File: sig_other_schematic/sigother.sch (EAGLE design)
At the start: 173 parts, among them IC1 DS3231/SO, IC4 MCP2300X/P, IC5 FT232RLSSOP, K1 TF2-L2-5V, K10 TF2-L2-5V, K11 TF2-L2-5V, K12 TF2-L2-5V, K13 TF2-L2-5V, K14 TF2-L2-5V, K2 TF2-L2-5V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

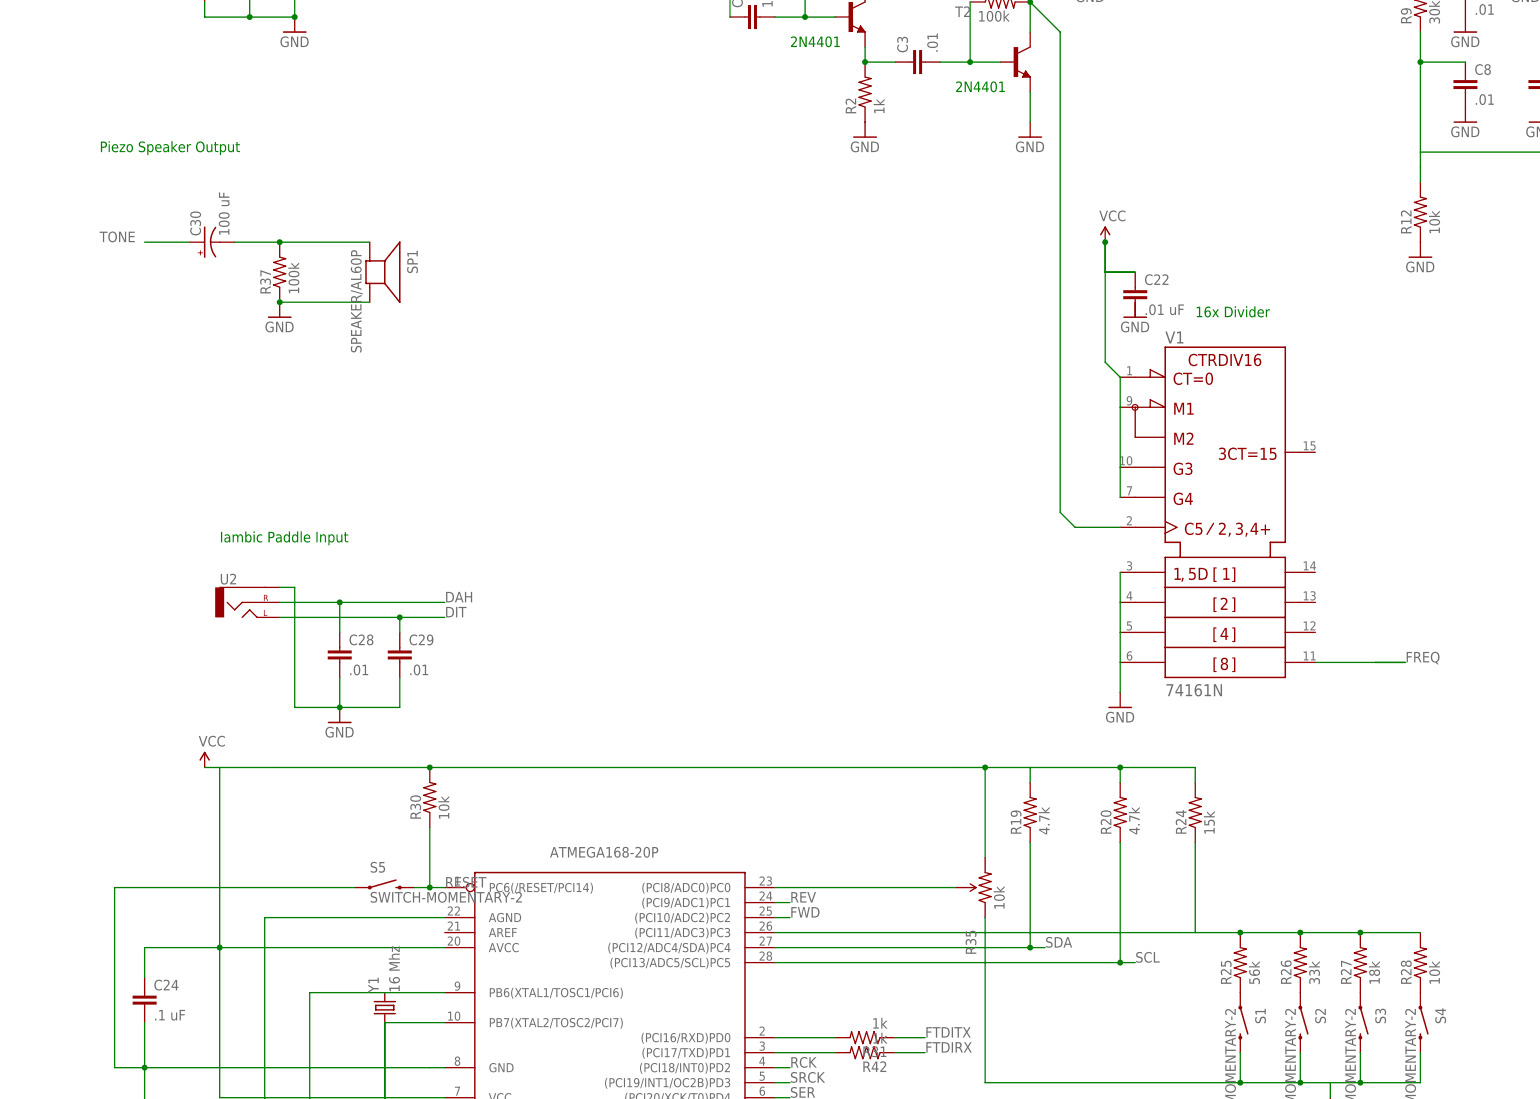
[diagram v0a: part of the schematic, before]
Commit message: updated command button layout (also speaker)
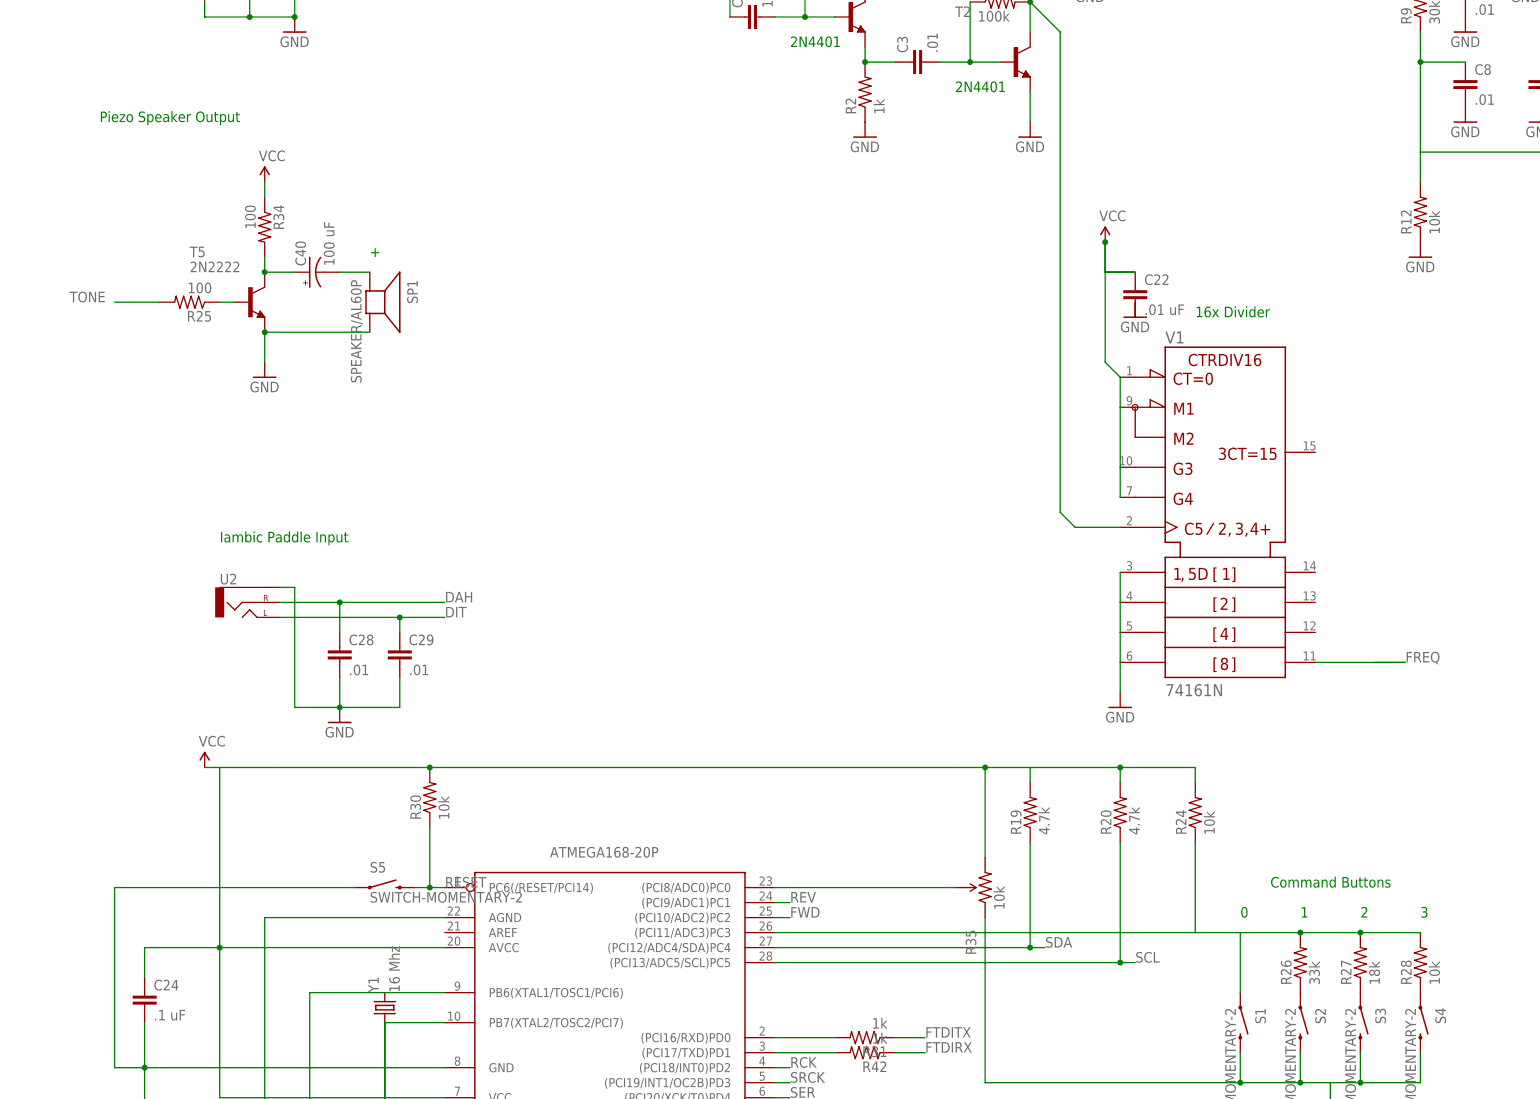
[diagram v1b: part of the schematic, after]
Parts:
- removed C30: 100 uF, SparkFun:CAP_POLPTH1
- removed R37: 100k, SparkFun:RESISTORPTH-1/4W
- added C40: 100 uF, SparkFun:CAP_POLPTH1
- added R34: 100, SparkFun:RESISTORPTH-1/4W
- added T5: 2N2222, adafruit:2N2222
- R24: value 15k -> 10k
- R25: value 56k -> 100
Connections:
- new net N$93: C40.-, SP1.+
- net GND: now also T5.E; no longer R37.1
- net N$104: now also C40.+, R34.2, T5.C; no longer C30.-, R37.2, SP1.+
- net N$12: now also S1.1; no longer R25.2
- net N$65: now also T5.B; no longer S1.1
- net TONE: now also R25.2; no longer C30.+
- net VCC: now also R34.1
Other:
- note added: "+"
- note added: "0"
- note added: "1"
- note added: "2"
- note added: "3"
- note added: "Command Buttons"
- moved on the sheet: R25, SP1
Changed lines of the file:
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@@
 <part name="TPIC6B595" library="ic-package" deviceset="DIL20" device=""/>
 <part name="S1" library="SparkFun" deviceset="SWITCH-MOMENTARY-2" device=""/>
-<part name="R25" library="SparkFun" deviceset="RESISTOR" device="PTH-1/4W" value="56k"/>
 <part name="R26" library="SparkFun" deviceset="RESISTOR" device="PTH-1/4W" value="33k"/>
 <part name="R27" library="SparkFun" deviceset="RESISTOR" device="PTH-1/4W" value="18k"/>
@@
 <part name="R19" library="SparkFun" deviceset="RESISTOR" device="PTH-1/4W" value="4.7k"/>
 <part name="R20" library="SparkFun" deviceset="RESISTOR" device="PTH-1/4W" value="4.7k"/>
-<part name="R24" library="SparkFun" deviceset="RESISTOR" device="PTH-1/4W" value="15k"/>
+<part name="R24" library="SparkFun" deviceset="RESISTOR" device="PTH-1/4W" value="10k"/>
 <part name="U2" library="SparkFun" deviceset="AUDIO-JACK" device="SMD2"/>
 <part name="R29" library="SparkFun" deviceset="RESISTOR" device="PTH-1/4W" value="4.7k"/>
@@
 <part name="GND33" library="SparkFun" deviceset="GND" device=""/>
 <part name="SP1" library="adafruit" deviceset="SPEAKER" device="/AL60P"/>
-<part name="C30" library="SparkFun" deviceset="CAP_POL" device="PTH1" value="100 uF"/>
-<part name="R37" library="SparkFun" deviceset="RESISTOR" device="PTH-1/4W" value="100k"/>
 <part name="GND34" library="SparkFun" deviceset="GND" device=""/>
 <part name="U$3" library="adafruit" deviceset="LT1302" device=""/>
@@
 <part name="R42" library="SparkFun" deviceset="RESISTOR" device="PTH-1/4W" value="1k"/>
 <part name="C39" library="SparkFun" deviceset="CAP" device="KIT" value=".1 uF"/>
+<part name="T5" library="adafruit" deviceset="2N2222" device=""/>
+<part name="C40" library="SparkFun" deviceset="CAP_POL" device="PTH1" value="100 uF"/>
+<part name="R25" library="SparkFun" deviceset="RESISTOR" device="PTH-1/4W" value="100"/>
+<part name="P+10" library="SparkFun" deviceset="VCC" device=""/>
+<part name="R34" library="SparkFun" deviceset="RESISTOR" device="PTH-1/4W" value="100"/>
 </parts>
 <sheets>
@@
 <text x="-154.94" y="-40.64" size="1.778" layer="91">Iambic Paddle Input</text>
 <text x="111.76" y="-88.9" size="1.778" layer="91">USB-Serial Interface</text>
-<text x="-175.26" y="25.4" size="1.778" layer="91">Piezo Speaker Output</text>
+<text x="-175.26" y="30.48" size="1.778" layer="91">Piezo Speaker Output</text>
 <text x="-127" y="180.34" size="1.778" layer="91">NC</text>
 <text x="180.34" y="-30.48" size="1.778" layer="91">8 pin: </text>
@@
 <text x="180.34" y="-43.18" size="1.778" layer="91">7: SDA</text>
 <text x="180.34" y="-45.72" size="1.778" layer="91">8: SCL</text>
+<text x="17.78" y="-104.14" size="1.778" layer="91">0</text>
+<text x="27.94" y="-104.14" size="1.778" layer="91">1</text>
+<text x="38.1" y="-104.14" size="1.778" layer="91">2</text>
+<text x="48.26" y="-104.14" size="1.778" layer="91">3</text>
+<text x="22.86" y="-99.06" size="1.778" layer="91">Command Buttons</text>
+<text x="-129.54" y="7.62" size="1.778" layer="91">+</text>
 </plain>
 <instances>
@@
 <instance part="TPIC6B595" gate="G$1" x="144.78" y="35.56"/>
 <instance part="S1" gate="G$1" x="17.78" y="-121.92" rot="R270"/>
-<instance part="R25" gate="G$1" x="17.78" y="-111.76" rot="R90"/>
 <instance part="R26" gate="G$1" x="27.94" y="-111.76" rot="R90"/>
 <instance part="R27" gate="G$1" x="38.1" y="-111.76" rot="R90"/>
@@
 <instance part="C29" gate="G$1" x="-124.46" y="-60.96"/>
 <instance part="GND33" gate="1" x="-134.62" y="-71.12"/>
-<instance part="SP1" gate="S1" x="-129.54" y="5.08" rot="R270"/>
-<instance part="C30" gate="G$1" x="-157.48" y="10.16" rot="R90"/>
-<instance part="R37" gate="G$1" x="-144.78" y="5.08" rot="R90"/>
-<instance part="GND34" gate="1" x="-144.78" y="-2.54"/>
+<instance part="SP1" gate="S1" x="-129.54" y="0" rot="R270"/>
+<instance part="GND34" gate="1" x="-147.32" y="-12.7"/>
 <instance part="U$3" gate="G$1" x="-132.08" y="165.1"/>
 <instance part="R38" gate="G$1" x="-129.54" y="132.08" rot="R90"/>
@@
 <instance part="R42" gate="G$1" x="-45.72" y="-127" rot="R180"/>
 <instance part="C39" gate="G$1" x="215.9" y="-127" rot="R90"/>
+<instance part="T5" gate="G$1" x="-149.86" y="0"/>
+<instance part="C40" gate="G$1" x="-139.7" y="5.08" rot="R90"/>
+<instance part="R25" gate="G$1" x="-160.02" y="0" rot="R180"/>
+<instance part="P+10" gate="1" x="-147.32" y="20.32"/>
+<instance part="R34" gate="G$1" x="-147.32" y="12.7" rot="R270"/>
 </instances>
 <busses>
@@
 <junction x="-134.62" y="-68.58"/>
 <pinref part="GND33" gate="1" pin="GND"/>
-</segment>
-<segment>
-<pinref part="SP1" gate="S1" pin="-"/>
-<wire x1="-129.54" y1="0" x2="-144.78" y2="0" width="0.2032" layer="91"/>
-<pinref part="R37" gate="G$1" pin="1"/>
-<pinref part="GND34" gate="1" pin="GND"/>
-<junction x="-144.78" y="0"/>
 </segment>
 <segment>
@@
 <junction x="-134.62" y="190.5"/>
 </segment>
+<segment>
+<pinref part="T5" gate="G$1" pin="E"/>
+<pinref part="GND34" gate="1" pin="GND"/>
+<wire x1="-147.32" y1="-5.08" x2="-147.32" y2="-10.16" width="0.2032" layer="91"/>
+<pinref part="SP1" gate="S1" pin="-"/>
+<wire x1="-129.54" y1="-5.08" x2="-147.32" y2="-5.08" width="0.2032" layer="91"/>
+<junction x="-147.32" y="-5.08"/>
+</segment>
 </net>
 <net name="N$6" class="0">
@@
 <junction x="154.94" y="-134.62"/>
 </segment>
+<segment>
+<pinref part="P+10" gate="1" pin="VCC"/>
+<pinref part="R34" gate="G$1" pin="1"/>
+<wire x1="-147.32" y1="20.32" x2="-147.32" y2="17.78" width="0.1524" layer="91"/>
+</segment>
 </net>
 <net name="N$10" class="0">
@@
 <wire x1="-60.96" y1="-106.68" x2="7.62" y2="-106.68" width="0.2032" layer="91"/>
 <wire x1="7.62" y1="-106.68" x2="10.16" y2="-106.68" width="0.2032" layer="91"/>
-<pinref part="R25" gate="G$1" pin="2"/>
 <wire x1="10.16" y1="-106.68" x2="17.78" y2="-106.68" width="0.2032" layer="91"/>
 <wire x1="17.78" y1="-106.68" x2="27.94" y2="-106.68" width="0.2032" layer="91"/>
-<junction x="17.78" y="-106.68"/>
 <pinref part="R26" gate="G$1" pin="2"/>
 <wire x1="27.94" y1="-106.68" x2="38.1" y2="-106.68" width="0.2032" layer="91"/>
@@
 <wire x1="10.16" y1="-106.68" x2="10.16" y2="-91.44" width="0.2032" layer="91"/>
 <pinref part="R24" gate="G$1" pin="1"/>
-</segment>
-</net>
-<net name="N$65" class="0">
-<segment>
-<pinref part="R25" gate="G$1" pin="1"/>
 <pinref part="S1" gate="G$1" pin="1"/>
+<wire x1="17.78" y1="-116.84" x2="17.78" y2="-106.68" width="0.2032" layer="91"/>
 </segment>
 </net>
@@
 </segment>
 <segment>
-<pinref part="C30" gate="G$1" pin="+"/>
-<wire x1="-160.02" y1="10.16" x2="-167.64" y2="10.16" width="0.2032" layer="91"/>
-<label x="-175.26" y="10.16" size="1.778" layer="95"/>
-</segment>
-</net>
-<net name="N$104" class="0">
-<segment>
-<pinref part="SP1" gate="S1" pin="+"/>
-<wire x1="-129.54" y1="10.16" x2="-144.78" y2="10.16" width="0.2032" layer="91"/>
-<pinref part="C30" gate="G$1" pin="-"/>
-<pinref part="R37" gate="G$1" pin="2"/>
-<wire x1="-144.78" y1="10.16" x2="-152.4" y2="10.16" width="0.2032" layer="91"/>
-<junction x="-144.78" y="10.16"/>
+<wire x1="-165.1" y1="0" x2="-172.72" y2="0" width="0.2032" layer="91"/>
+<label x="-180.34" y="0" size="1.778" layer="95"/>
+<pinref part="R25" gate="G$1" pin="2"/>
 </segment>
 </net>
@@
 </segment>
 </net>
+<net name="N$65" class="0">
+<segment>
+<pinref part="R25" gate="G$1" pin="1"/>
+<pinref part="T5" gate="G$1" pin="B"/>
+<wire x1="-154.94" y1="0" x2="-152.4" y2="0" width="0.2032" layer="91"/>
+</segment>
+</net>
+<net name="N$93" class="0">
+<segment>
+<pinref part="C40" gate="G$1" pin="-"/>
+<pinref part="SP1" gate="S1" pin="+"/>
+<wire x1="-134.62" y1="5.08" x2="-129.54" y2="5.08" width="0.2032" layer="91"/>
+</segment>
+</net>
+<net name="N$104" class="0">
+<segment>
+<pinref part="R34" gate="G$1" pin="2"/>
+<pinref part="T5" gate="G$1" pin="C"/>
+<wire x1="-147.32" y1="7.62" x2="-147.32" y2="5.08" width="0.2032" layer="91"/>
+<pinref part="C40" gate="G$1" pin="+"/>
+<wire x1="-147.32" y1="5.08" x2="-142.24" y2="5.08" width="0.2032" layer="91"/>
+<junction x="-147.32" y="5.08"/>
+</segment>
+</net>
